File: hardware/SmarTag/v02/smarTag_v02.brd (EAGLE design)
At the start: 33 x 40.6 mm, 21 parts, among them U1 ADXL362

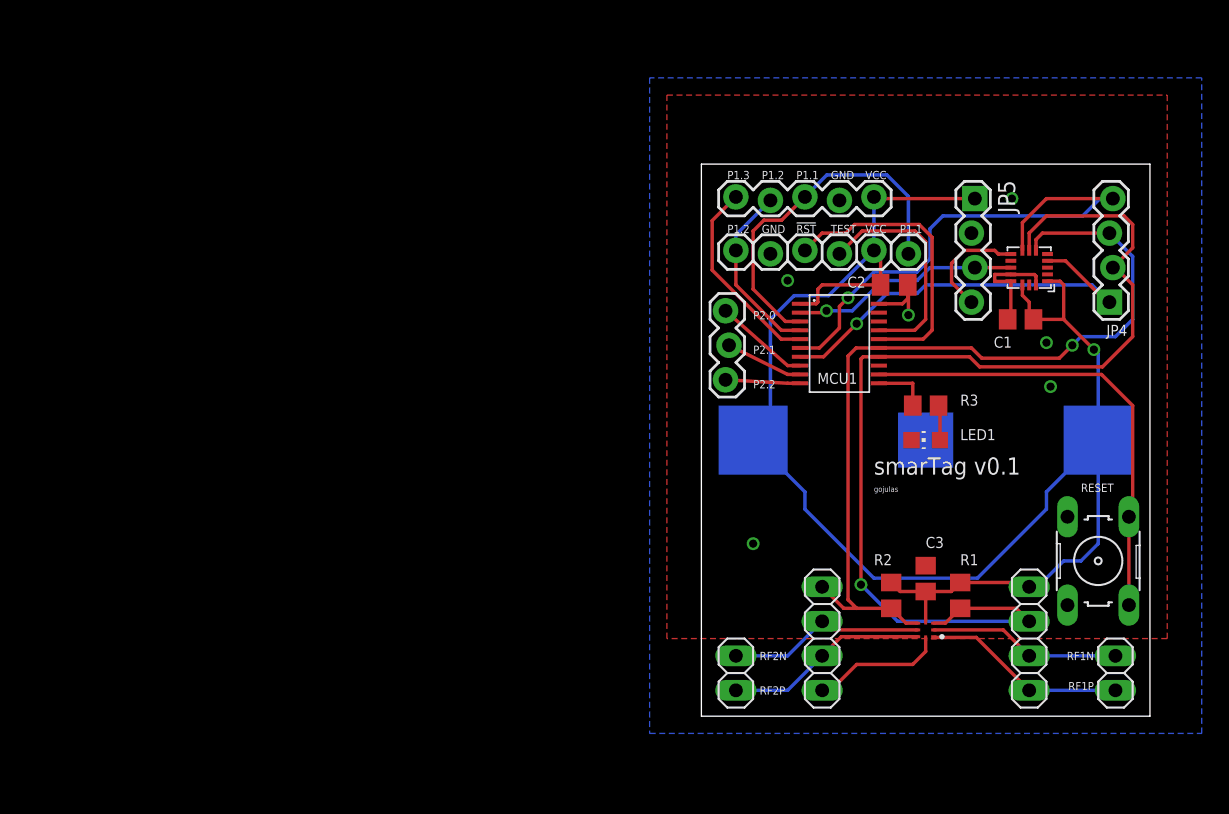
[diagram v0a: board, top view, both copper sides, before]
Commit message: hw: Remove JP4-7 from schematic. Add basic board.
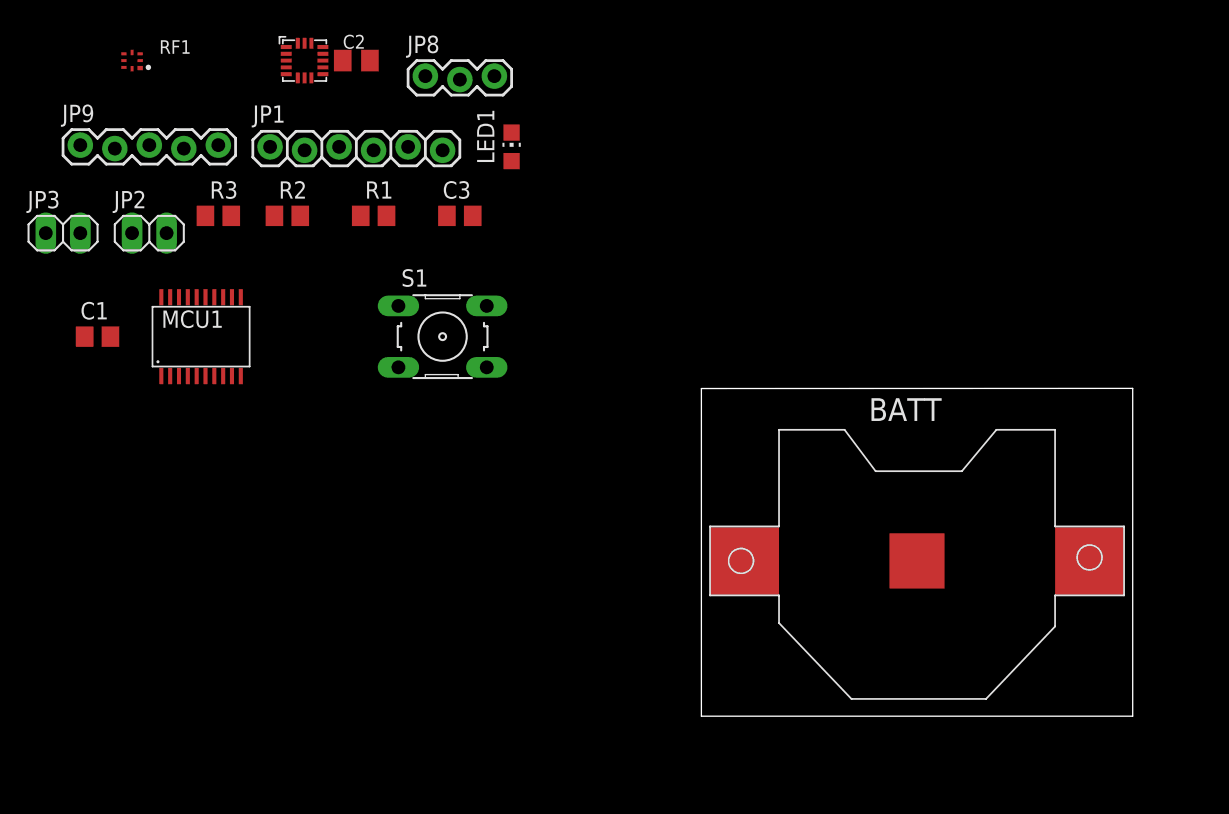
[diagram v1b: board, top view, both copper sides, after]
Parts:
- removed JP4, JP5: (no value), SparkFun-Connectors:1X04_LOCK
- removed JP6, JP7: (no value), pinhead:1X04
- moved JP2 78.1 mm to (-40.6, 35.6), turned to 0 degrees
- moved RF1 71.9 mm to (-41.9, 48.3)
- moved C1 68.0 mm to (-44.5, 27.9), turned to 0 degrees
- moved JP3 59.2 mm to (-47.0, 35.6), turned to 0 degrees
- moved U1 55.5 mm to (-29.2, 48.3), turned to 0 degrees
- moved R3 53.9 mm to (-35.6, 36.8)
- moved R2 52.5 mm to (-30.5, 36.8), turned to 0 degrees
- moved R1 51.4 mm to (-24.1, 36.8), turned to 0 degrees
- moved S1 51.0 mm to (-19.1, 27.9), turned to 0 degrees
- moved JP9 48.4 mm to (-45.7, 41.9)
- moved MCU1 47.0 mm to (-36.8, 27.9), turned to 0 degrees
- moved C3 43.5 mm to (-17.8, 36.8), turned to 0 degrees
- moved C2 42.9 mm to (-25.4, 48.3)
- moved LED1 37.4 mm to (-14.0, 41.9), turned to 0 degrees
- moved JP1 35.1 mm to (-31.8, 41.9)
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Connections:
- net GND: no longer JP5.2, JP7.1
- net INT2: no longer JP5.4
- net P1.0: no longer JP5.3
- net P1.4: no longer JP4.4
- net P1.5: no longer JP4.1
- net P1.6: no longer JP4.2, JP6.3
- net P1.7: no longer JP4.3, JP7.4
- net RF1N: no longer JP6.2
- net RF1P: no longer JP6.1
- net RF2N: no longer JP7.3
- net RF2P: no longer JP7.2
- net VCC: no longer JP5.1, JP6.4
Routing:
- net VCC: track 122.1 -> 0.00 mm, vias 1 -> 0
- net P1.6: track 78.5 -> 0.00 mm, vias 1 -> 0
- net P1.7: track 63.1 -> 0.00 mm, vias 1 -> 0
- net P1.4: track 39.2 -> 0.00 mm, vias 1 -> 0
- net P2.4: track 34.4 -> 0.00 mm
- net P1.5: track 31.3 -> 0.00 mm, vias 1 -> 0
- net P1.1/RX: track 26.7 -> 0.00 mm
- net GND: track 25.5 -> 0.00 mm, vias 6 -> 0
- net !RST: track 21.6 -> 0.00 mm
- net P1.0: track 16.9 -> 0.00 mm, vias 1 -> 0
- net TEST: track 16.9 -> 0.00 mm
- net RF2P: track 15.0 -> 0.00 mm
- net RF1P: track 15.0 -> 0.00 mm
- net RF2N: track 14.7 -> 0.00 mm
- net P1.3: track 14.7 -> 0.00 mm
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- removed copper zone on layer 1, net GND
- removed copper zone on layer 16, net GND
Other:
- board size 33 x 40.6 mm -> 31.8 x 24.1 mm
- board text removed: "!RST"
- board text removed: "GND"
- board text removed: "P1.1"
- board text removed: "P1.2"
- board text removed: "P1.3"
- board text removed: "P2.0"
- board text removed: "P2.1"
- board text removed: "P2.2"
- board text removed: "RESET"
- board text removed: "RF1N"
- board text removed: "RF1P"
- board text removed: "RF2N"
- board text removed: "RF2P"
- board text removed: "TEST"
- board text removed: "VCC"
- board text removed: "gojulas"
- board text removed: "smarTag v0.1"

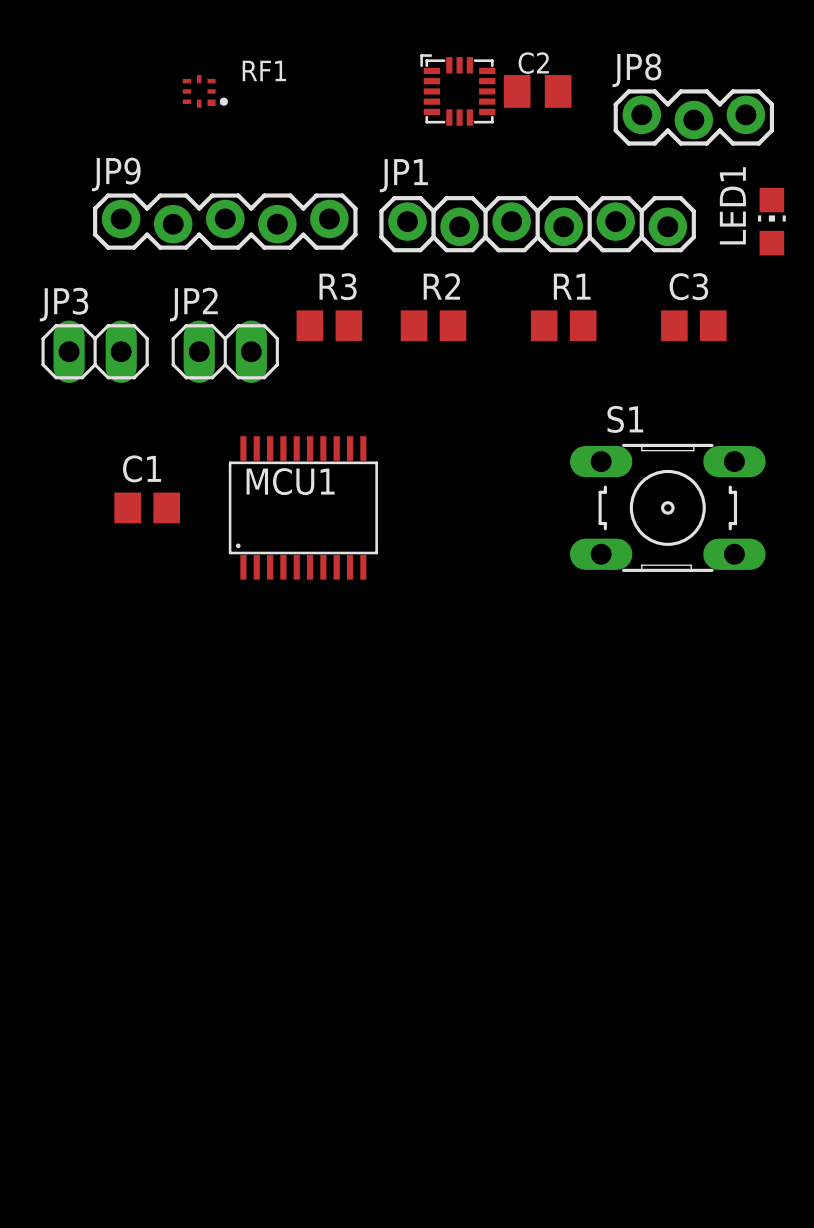
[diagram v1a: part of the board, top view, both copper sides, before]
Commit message: hw: Renumber JP headers and fix BT header.
Remove P1.3 signal from BT daughter board header.
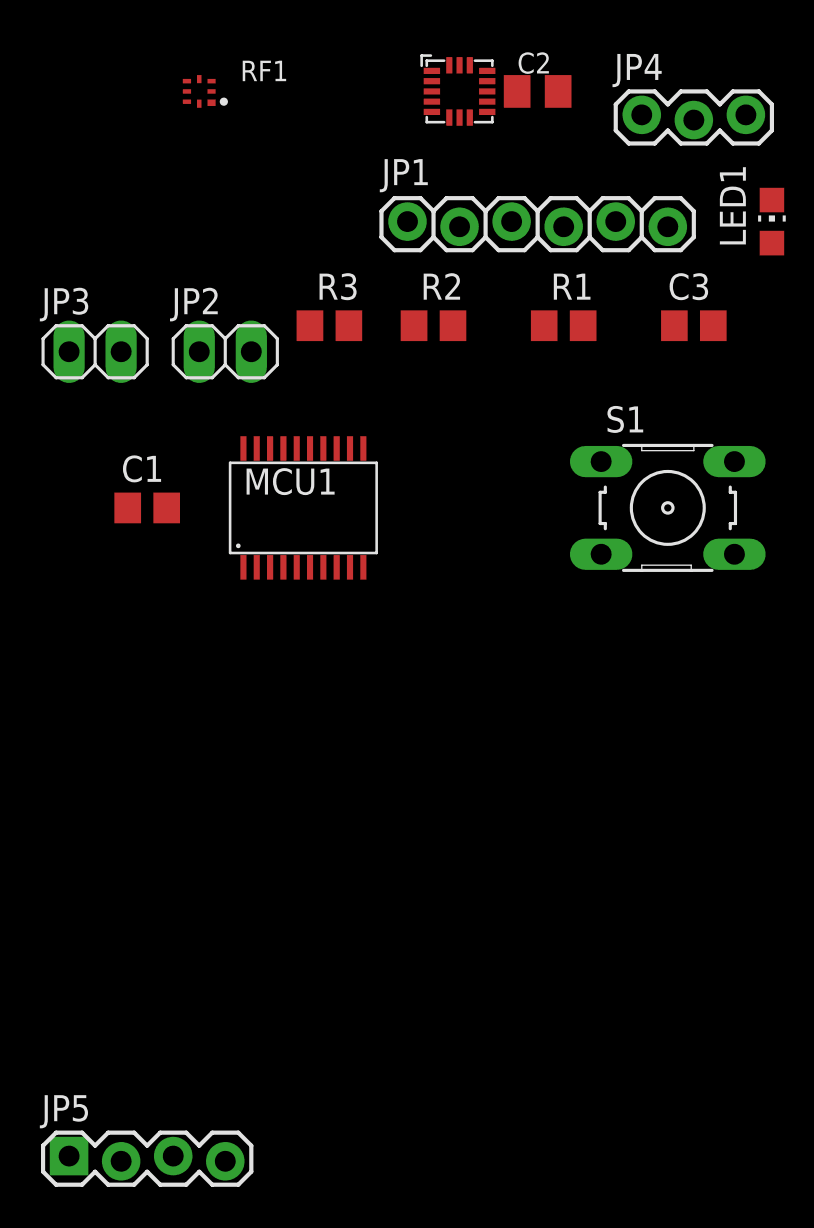
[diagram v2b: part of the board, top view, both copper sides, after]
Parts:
- removed JP9: (no value), SparkFun-Connectors:1X05_LOCK
- added JP5: (no value), SparkFun-Connectors:1X04_LOCK
- renumbered JP8 to JP4
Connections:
- net GND: now also JP5.3; no longer JP9.4
- net P1.1/RX: now also JP5.2; no longer JP9.3
- net P1.2/TX: now also JP5.1; no longer JP9.2
- net P1.3: no longer JP9.1
- net VCC: now also JP5.4; no longer JP9.5
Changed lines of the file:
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@@
 <element name="JP2" library="pinhead" package="1X02" value="" x="-40.64" y="35.56"/>
 <element name="JP3" library="pinhead" package="1X02" value="" x="-46.99" y="35.56"/>
-<element name="JP8" library="SparkFun-Connectors" package="1X03_LOCK" value="" x="-20.32" y="46.99"/>
-<element name="JP9" library="SparkFun-Connectors" package="1X05_LOCK" value="" x="-45.72" y="41.91"/>
+<element name="JP4" library="SparkFun-Connectors" package="1X03_LOCK" value="" x="-20.32" y="46.99"/>
 <element name="LED1" library="led" package="CHIP-LED0805" value="" x="-13.97" y="41.91"/>
 <element name="MCU1" library="TI_MSP430_v16" package="PW20" value="G2X[1/5]2---PW20" x="-36.83" y="27.94"/>
@@
 <element name="U1" library="SparkFun-Sensors" package="ADXL362" value="ADXL362" x="-29.21" y="48.26">
 <attribute name="PROD_ID" value="IC-11297" x="-29.21" y="48.26" size="1.778" layer="27" display="off"/>
+</element>
+<element name="JP5" library="SparkFun-Connectors" package="1X04_LOCK" value="" x="-48.26" y="-3.81">
+<attribute name="PROD_ID" value="CONN-09696" x="-48.26" y="-3.81" size="1.778" layer="27" display="off"/>
 </element>
 </elements>
@@
 <contactref element="BATT" pad="+$1"/>
 <contactref element="BATT" pad="+$2"/>
-<contactref element="JP9" pad="5"/>
-<wire x1="-39.7549" y1="25.0399" x2="3.175" y2="11.43" width="0" layer="19" extent="1-1"/>
+<contactref element="JP5" pad="4"/>
+<wire x1="-39.7549" y1="25.0399" x2="-40.64" y2="-3.937" width="0" layer="19" extent="1-1"/>
 <wire x1="-45.4" y1="27.94" x2="-39.7549" y2="25.0399" width="0" layer="19" extent="1-1"/>
 <wire x1="-31.43" y1="36.83" x2="-39.7549" y2="25.0399" width="0" layer="19" extent="1-1"/>
@@
 <wire x1="-21.59" y1="41.91" x2="-25.08" y2="36.83" width="0" layer="19" extent="1-1"/>
 <wire x1="-18.73" y1="36.83" x2="-21.59" y2="41.91" width="0" layer="19" extent="1-1"/>
-<wire x1="-35.56" y1="42.037" x2="-31.43" y2="36.83" width="0" layer="19" extent="1-1"/>
 <wire x1="-26.4" y1="48.26" x2="-21.59" y2="41.91" width="0" layer="19" extent="1-1"/>
 <wire x1="-28.71" y1="49.535" x2="-26.4" y2="48.26" width="0" layer="19" extent="1-1"/>
 <wire x1="-30.56" y1="49.26" x2="-28.71" y2="49.535" width="0" layer="19" extent="1-1"/>
-<wire x1="-41.91" y1="48.86" x2="-35.56" y2="42.037" width="0" layer="19" extent="1-1"/>
+<wire x1="-41.91" y1="48.86" x2="-30.56" y2="49.26" width="0" layer="19" extent="1-1"/>
+<wire x1="3.175" y1="11.43" x2="-18.73" y2="36.83" width="0" layer="19" extent="1-1"/>
 <wire x1="28.575" y1="11.43" x2="3.175" y2="11.43" width="0" layer="19" extent="1-1"/>
 </signal>
@@
 <contactref element="MCU1" pad="3"/>
 <contactref element="JP1" pad="6"/>
-<contactref element="JP9" pad="3"/>
-<wire x1="-40.64" y1="42.037" x2="-19.05" y2="41.656" width="0" layer="19" extent="1-1"/>
-<wire x1="-38.455" y1="25.0399" x2="-40.64" y2="42.037" width="0" layer="19" extent="1-1"/>
+<contactref element="JP5" pad="2"/>
+<wire x1="-38.455" y1="25.0399" x2="-45.72" y2="-3.937" width="0" layer="19" extent="1-1"/>
+<wire x1="-19.05" y1="41.656" x2="-38.455" y2="25.0399" width="0" layer="19" extent="1-1"/>
 </signal>
 <signal name="P1.2/TX">
 <contactref element="MCU1" pad="4"/>
 <contactref element="JP1" pad="1"/>
-<contactref element="JP9" pad="2"/>
-<wire x1="-43.18" y1="41.783" x2="-37.805" y2="25.0399" width="0" layer="19" extent="1-1"/>
-<wire x1="-31.75" y1="41.91" x2="-43.18" y2="41.783" width="0" layer="19" extent="1-1"/>
+<contactref element="JP5" pad="1"/>
+<wire x1="-37.805" y1="25.0399" x2="-48.26" y2="-3.683" width="0" layer="19" extent="1-1"/>
+<wire x1="-31.75" y1="41.91" x2="-37.805" y2="25.0399" width="0" layer="19" extent="1-1"/>
 </signal>
 <signal name="P1.4">
@@
 <signal name="P2.0_C" class="1">
 <contactref element="MCU1" pad="8"/>
-<contactref element="JP8" pad="3"/>
+<contactref element="JP4" pad="3"/>
 <wire x1="-35.205" y1="25.0399" x2="-15.24" y2="47.117" width="0" layer="19" extent="1-1"/>
 </signal>
 <signal name="P2.1_C" class="1">
 <contactref element="MCU1" pad="9"/>
-<contactref element="JP8" pad="2"/>
+<contactref element="JP4" pad="2"/>
 <wire x1="-34.555" y1="25.0399" x2="-17.78" y2="46.863" width="0" layer="19" extent="1-1"/>
 </signal>
 <signal name="P2.2_C" class="1">
 <contactref element="MCU1" pad="10"/>
-<contactref element="JP8" pad="1"/>
+<contactref element="JP4" pad="1"/>
 <wire x1="-33.9051" y1="25.0399" x2="-20.32" y2="47.117" width="0" layer="19" extent="1-1"/>
 </signal>
@@
 <contactref element="BATT" pad="-"/>
 <contactref element="LED1" pad="C"/>
-<contactref element="JP9" pad="4"/>
 <contactref element="S1" pad="1"/>
 <contactref element="S1" pad="2"/>
 <contactref element="C2" pad="2"/>
 <contactref element="MCU1" pad="20"/>
+<contactref element="JP5" pad="3"/>
+<wire x1="-43.5" y1="27.94" x2="-43.18" y2="-3.683" width="0" layer="19" extent="1-1"/>
+<wire x1="-39.7549" y1="30.84" x2="-43.5" y2="27.94" width="0" layer="19" extent="1-1"/>
+<wire x1="-29.21" y1="41.656" x2="-39.7549" y2="30.84" width="0" layer="19" extent="1-1"/>
+<wire x1="-27.86" y1="48.76" x2="-29.21" y2="41.656" width="0" layer="19" extent="1-1"/>
+<wire x1="-27.86" y1="49.26" x2="-27.86" y2="48.76" width="0" layer="19" extent="1-1"/>
+<wire x1="-29.71" y1="49.535" x2="-27.86" y2="49.26" width="0" layer="19" extent="1-1"/>
+<wire x1="-24.4" y1="48.26" x2="-27.86" y2="48.76" width="0" layer="19" extent="1-1"/>
+<wire x1="-13.97" y1="42.96" x2="-24.4" y2="48.26" width="0" layer="19" extent="1-1"/>
 <wire x1="-16.83" y1="36.83" x2="-13.97" y2="42.96" width="0" layer="19" extent="1-1"/>
 <wire x1="-15.7988" y1="30.2006" x2="-16.83" y2="36.83" width="0" layer="19" extent="1-1"/>
 <wire x1="-22.3012" y1="30.2006" x2="-15.7988" y2="30.2006" width="0" layer="19" extent="1-1"/>
-<wire x1="-24.4" y1="48.26" x2="-13.97" y2="42.96" width="0" layer="19" extent="1-1"/>
-<wire x1="-27.86" y1="48.76" x2="-24.4" y2="48.26" width="0" layer="19" extent="1-1"/>
-<wire x1="-27.86" y1="49.26" x2="-27.86" y2="48.76" width="0" layer="19" extent="1-1"/>
-<wire x1="-29.71" y1="49.535" x2="-27.86" y2="49.26" width="0" layer="19" extent="1-1"/>
-<wire x1="-29.21" y1="41.656" x2="-27.86" y2="48.76" width="0" layer="19" extent="1-1"/>
-<wire x1="-38.1" y1="41.783" x2="-29.21" y2="41.656" width="0" layer="19" extent="1-1"/>
-<wire x1="-41.91" y1="47.66" x2="-38.1" y2="41.783" width="0" layer="19" extent="1-1"/>
-<wire x1="-39.7549" y1="30.84" x2="-38.1" y2="41.783" width="0" layer="19" extent="1-1"/>
-<wire x1="-43.5" y1="27.94" x2="-39.7549" y2="30.84" width="0" layer="19" extent="1-1"/>
-<wire x1="15.875" y1="11.43" x2="-22.3012" y2="30.2006" width="0" layer="19" extent="1-1"/>
+<wire x1="-41.91" y1="47.66" x2="-29.71" y2="49.535" width="0" layer="19" extent="1-1"/>
+<wire x1="15.875" y1="11.43" x2="-15.7988" y2="30.2006" width="0" layer="19" extent="1-1"/>
 </signal>
 <signal name="RF1P">
@@
 </signal>
 <signal name="P1.3">
-<contactref element="JP9" pad="1"/>
 <contactref element="MCU1" pad="5"/>
-<wire x1="-45.72" y1="42.037" x2="-37.155" y2="25.0399" width="0" layer="19" extent="1-1"/>
 </signal>
 </signals>
